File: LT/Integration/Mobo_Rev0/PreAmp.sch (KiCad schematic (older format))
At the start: 8 parts, among them Q2 5486

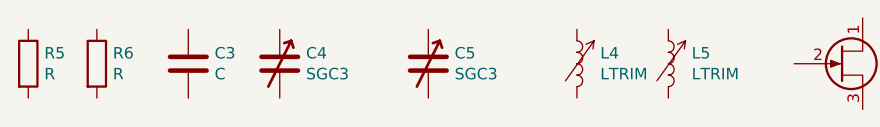
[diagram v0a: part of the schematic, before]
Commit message: I uploaded the schematics for the receiving stage into their respective hierarchial sheets and have begun the integration of the received stage
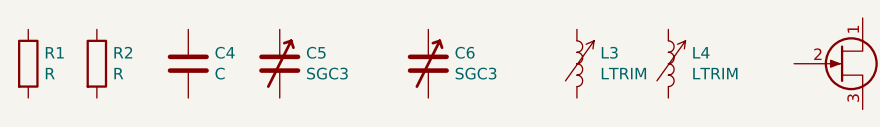
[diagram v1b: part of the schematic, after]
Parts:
- C4: renamed from C3; footprint Capacitor_SMD:C_0805_2012Metric -> (none)
- C5: renamed from C4; footprint LT:CAP_trimmer_SGC3_Download -> (none)
- C6: renamed from C5; footprint LT:CAP_trimmer_SGC3_Download -> (none)
- L3: renamed from L4; footprint LT:IND_trimmer_7M3 -> (none)
- L4: renamed from L5; footprint LT:IND_trimmer_7M3 -> (none)
- Q2: footprint Package_TO_SOT_SMD:TSOT-23 -> (none)
- renumbered R5 to R1, R6 to R2
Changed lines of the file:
@@
 $EndDescr
 $Comp
-L Device:R R5
+L Device:R R1
 U 1 1 5E4C437D
 P 2150 1950
-F 0 "R5" H 2220 1996 50  0000 L CNN
+F 0 "R1" H 2220 1996 50  0000 L CNN
 F 1 "R" H 2220 1905 50  0000 L CNN
 F 2 "Capacitor_SMD:C_0805_2012Metric" V 2080 1950 50  0001 C CNN
@@
 $EndComp
 $Comp
-L Device:R R6
+L Device:R R2
 U 1 1 5E4C43C9
 P 2450 1950
-F 0 "R6" H 2520 1996 50  0000 L CNN
+F 0 "R2" H 2520 1996 50  0000 L CNN
 F 1 "R" H 2520 1905 50  0000 L CNN
 F 2 "Capacitor_SMD:C_0805_2012Metric" V 2380 1950 50  0001 C CNN
@@
 $EndComp
 $Comp
-L Device:C C3
+L Device:C C4
 U 1 1 5E4C4423
 P 2850 1950
-F 0 "C3" H 2965 1996 50  0000 L CNN
+F 0 "C4" H 2965 1996 50  0000 L CNN
 F 1 "C" H 2965 1905 50  0000 L CNN
-F 2 "Capacitor_SMD:C_0805_2012Metric" H 2888 1800 50  0001 C CNN
+F 2 "" H 2888 1800 50  0001 C CNN
 F 3 "~" H 2850 1950 50  0001 C CNN
 	1    2850 1950
@@
 $EndComp
 $Comp
-L Device:C_Variable C4
+L Device:C_Variable C5
 U 1 1 5E4C44A9
 P 3250 1950
-F 0 "C4" H 3365 1996 50  0000 L CNN
+F 0 "C5" H 3365 1996 50  0000 L CNN
 F 1 "SGC3" H 3365 1905 50  0000 L CNN
-F 2 "LT:CAP_trimmer_SGC3_Download" H 3250 1950 50  0001 C CNN
+F 2 "" H 3250 1950 50  0001 C CNN
 F 3 "~" H 3250 1950 50  0001 C CNN
 	1    3250 1950
@@
 $EndComp
 $Comp
-L Device:C_Variable C5
+L Device:C_Variable C6
 U 1 1 5E4C44E9
 P 3900 1950
-F 0 "C5" H 4015 1996 50  0000 L CNN
+F 0 "C6" H 4015 1996 50  0000 L CNN
 F 1 "SGC3" H 4015 1905 50  0000 L CNN
-F 2 "LT:CAP_trimmer_SGC3_Download" H 3900 1950 50  0001 C CNN
+F 2 "" H 3900 1950 50  0001 C CNN
 F 3 "~" H 3900 1950 50  0001 C CNN
 	1    3900 1950
@@
 $EndComp
 $Comp
-L Device:LTRIM L4
+L Device:LTRIM L3
 U 1 1 5E4C4541
 P 4550 1950
-F 0 "L4" H 4652 1996 50  0000 L CNN
+F 0 "L3" H 4652 1996 50  0000 L CNN
 F 1 "LTRIM" H 4652 1905 50  0000 L CNN
-F 2 "LT:IND_trimmer_7M3" H 4550 1950 50  0001 C CNN
+F 2 "" H 4550 1950 50  0001 C CNN
 F 3 "~" H 4550 1950 50  0001 C CNN
 	1    4550 1950
@@
 $EndComp
 $Comp
-L Device:LTRIM L5
+L Device:LTRIM L4
 U 1 1 5E4C459D
 P 4950 1950
-F 0 "L5" H 5052 1996 50  0000 L CNN
+F 0 "L4" H 5052 1996 50  0000 L CNN
 F 1 "LTRIM" H 5052 1905 50  0000 L CNN
-F 2 "LT:IND_trimmer_7M3" H 4950 1950 50  0001 C CNN
+F 2 "" H 4950 1950 50  0001 C CNN
 F 3 "~" H 4950 1950 50  0001 C CNN
 	1    4950 1950
@@
 F 0 "Q2" H 5891 1996 50  0000 L CNN
 F 1 "5486" H 5891 1905 50  0000 L CNN
-F 2 "Package_TO_SOT_SMD:TSOT-23" H 5900 2050 50  0001 C CNN
+F 2 "" H 5900 2050 50  0001 C CNN
 F 3 "~" H 5700 1950 50  0001 C CNN
 	1    5700 1950

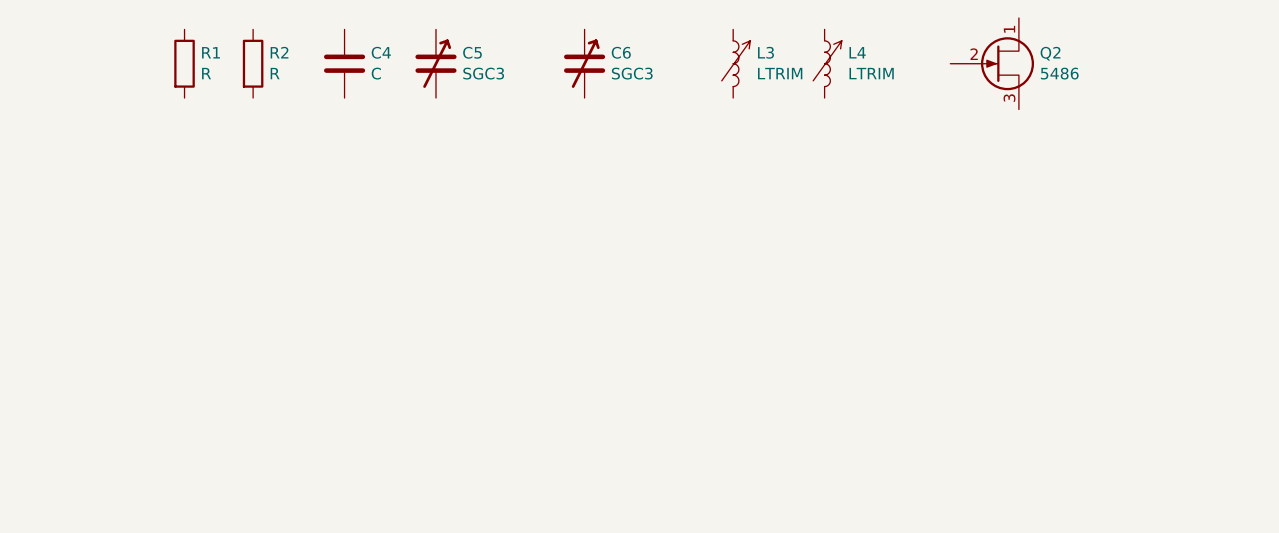
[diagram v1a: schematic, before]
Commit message: Finished a preliminary layout for the Receiving Stage, and uploaded the schematics for the Pre-Amp, 29.4 BPF, and 29.4 LPF.
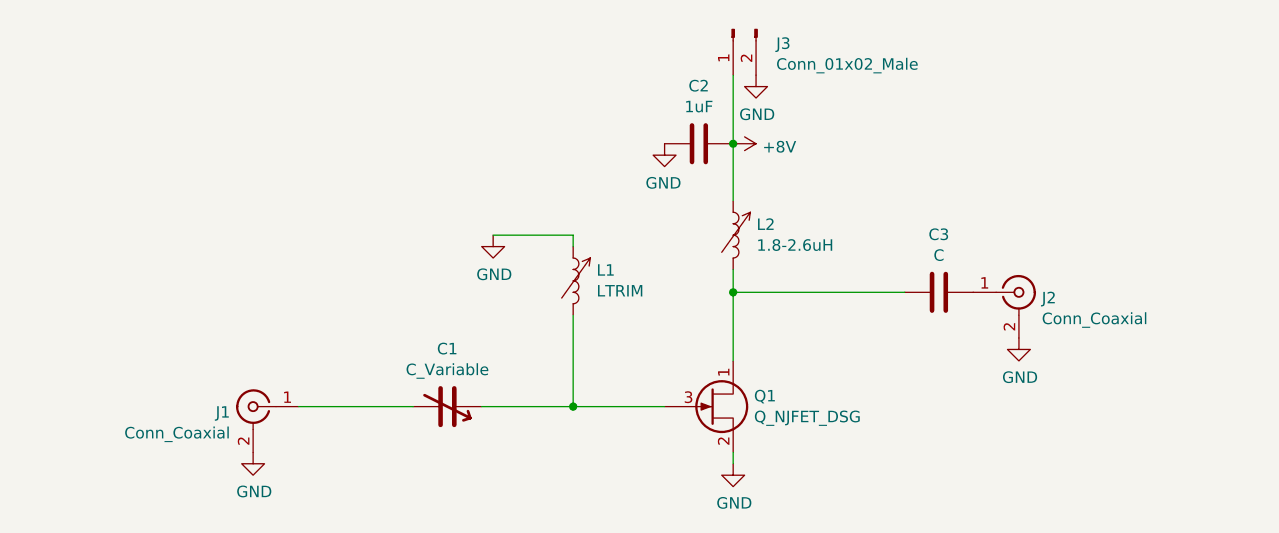
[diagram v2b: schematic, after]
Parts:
- removed C4: C, symbol Device:C
- removed C5, C6: SGC3, symbol Device:C_Variable
- removed L3, L4: LTRIM, symbol Device:LTRIM
- removed Q2: 5486, symbol Device:Q_NJFET_DGS
- removed R1, R2: R, Capacitor_SMD:C_0805_2012Metric, symbol Device:R
- added C1: C_Variable, LT:CAP_trimmer_SGC3_Download, symbol Device:C_Variable
- added C2: 1uF, Capacitor_SMD:C_0805_2012Metric_Pad1.15x1.40mm_HandSolder, symbol Device:C
- added C3: C, Capacitor_SMD:C_0805_2012Metric_Pad1.15x1.40mm_HandSolder, symbol Device:C
- added J1, J2: Conn_Coaxial, Connector_Coaxial:SMA_Amphenol_132289_EdgeMount, symbol Connector:Conn_Coaxial
- added J3: Conn_01x02_Male, Connector_PinHeader_2.54mm:PinHeader_1x02_P2.54mm_Vertical, symbol Connector:Conn_01x02_Male
- added L1: LTRIM, LT:IND_trimmer_7M3, symbol Device:LTRIM
- added L2: 1.8-2.6uH, LT:IND_trimmer_7M3, symbol Device:LTRIM
- added Q1: Q_NJFET_DSG, Package_TO_SOT_SMD:SOT-23, symbol Device:Q_NJFET_DSG
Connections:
- new net: C1.1, L1.2, Q1.3 (G)
- new net: C3.2, L2.2, Q1.1 (D)
- new net: C1.2, J1.1 (In)
- new net: C3.1, J2.1 (In)
- new net +8V: C2.1, J3.1 (Pin_1), L2.1
- new net GND: C2.2, J1.2 (Ext), J2.2 (Ext), J3.2 (Pin_2), L1.1, Q1.2 (S)

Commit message: Annotating components for Transmitting stage. In progress
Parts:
- renumbered C1 to C33, C2 to C34, C3 to C35
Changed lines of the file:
@@
 $Descr A4 11693 8268
 encoding utf-8
-Sheet 1 10
+Sheet 3 10
 Title ""
 Date ""
@@
 $EndComp
 $Comp
-L Device:C C2
+L Device:C C34
 U 1 1 5E544C2E
 P 4400 2300
-F 0 "C2" V 4652 2300 50  0000 C CNN
+F 0 "C34" V 4652 2300 50  0000 C CNN
 F 1 "1uF" V 4561 2300 50  0000 C CNN
 F 2 "Capacitor_SMD:C_0805_2012Metric_Pad1.15x1.40mm_HandSolder" H 4438 2150 50  0001 C CNN
@@
 $EndComp
 $Comp
-L Device:C_Variable C1
+L Device:C_Variable C33
 U 1 1 5E545231
 P 3300 3450
-F 0 "C1" V 3048 3450 50  0000 C CNN
+F 0 "C33" V 3048 3450 50  0000 C CNN
 F 1 "C_Variable" V 3139 3450 50  0000 C CNN
 F 2 "LT:CAP_trimmer_SGC3_Download" H 3300 3450 50  0001 C CNN
@@
 Connection ~ 3850 3450
 $Comp
-L Device:C C3
+L Device:C C35
 U 1 1 5E54F603
 P 5450 2950
-F 0 "C3" V 5198 2950 50  0000 C CNN
+F 0 "C35" V 5198 2950 50  0000 C CNN
 F 1 "C" V 5289 2950 50  0000 C CNN
 F 2 "Capacitor_SMD:C_0805_2012Metric_Pad1.15x1.40mm_HandSolder" H 5488 2800 50  0001 C CNN

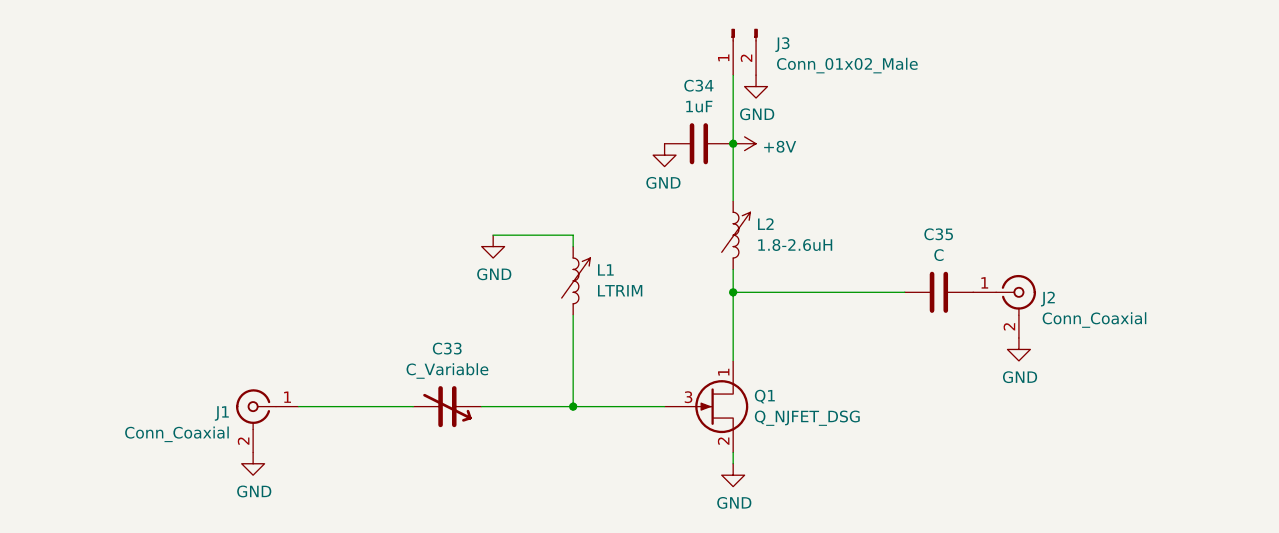
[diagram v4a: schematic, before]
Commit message: Transmitting stage annotations are done. Ready to layout PCB for rev0
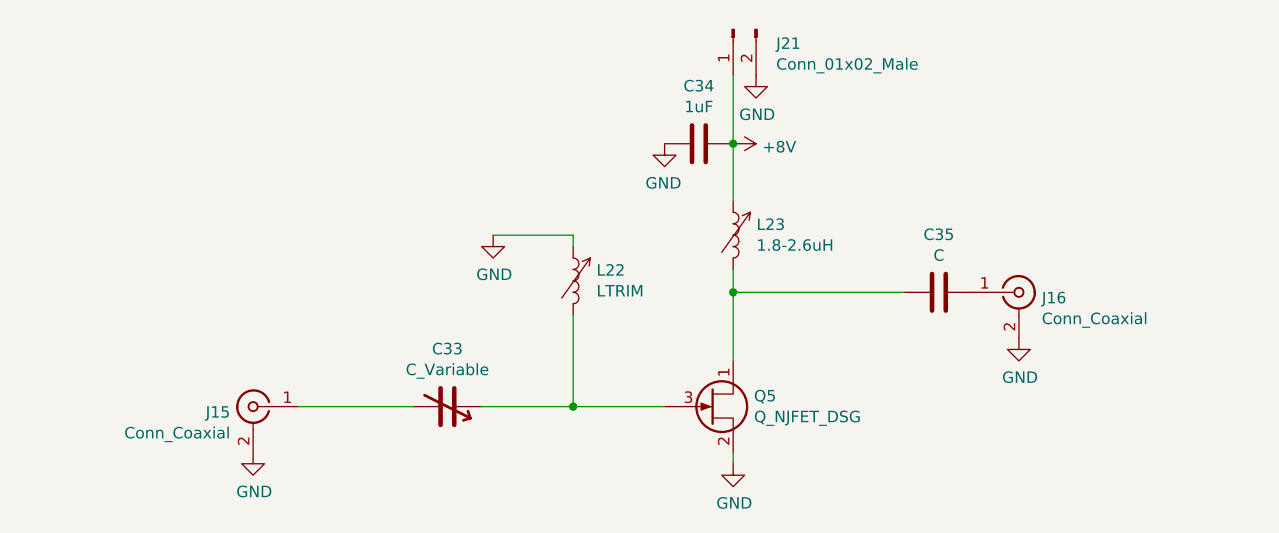
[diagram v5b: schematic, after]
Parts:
- renumbered J1 to J15, J2 to J16, J3 to J21, L1 to L22, L2 to L23, Q1 to Q5
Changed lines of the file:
@@
 $EndDescr
 $Comp
-L Device:LTRIM L1
+L Device:LTRIM L22
 U 1 1 5E543F18
 P 3850 2900
-F 0 "L1" H 3952 2946 50  0000 L CNN
+F 0 "L22" H 3952 2946 50  0000 L CNN
 F 1 "LTRIM" H 3952 2855 50  0000 L CNN
 F 2 "LT:IND_trimmer_7M3" H 3850 2900 50  0001 C CNN
@@
 $EndComp
 $Comp
-L Device:LTRIM L2
+L Device:LTRIM L23
 U 1 1 5E54443E
 P 4550 2700
-F 0 "L2" H 4652 2746 50  0000 L CNN
+F 0 "L23" H 4652 2746 50  0000 L CNN
 F 1 "1.8-2.6uH" H 4652 2655 50  0000 L CNN
 F 2 "LT:IND_trimmer_7M3" H 4550 2700 50  0001 C CNN
@@
 $EndComp
 $Comp
-L Connector:Conn_Coaxial J1
+L Connector:Conn_Coaxial J15
 U 1 1 5E546B8B
 P 2450 3450
-F 0 "J1" H 2550 3425 50  0000 L CNN
+F 0 "J15" H 2550 3425 50  0000 L CNN
 F 1 "Conn_Coaxial" H 2550 3334 50  0000 L CNN
 F 2 "Connector_Coaxial:SMA_Amphenol_132289_EdgeMount" H 2450 3450 50  0001 C CNN
@@
 $EndComp
 $Comp
-L Connector:Conn_Coaxial J2
+L Connector:Conn_Coaxial J16
 U 1 1 5E547249
 P 5800 2950
-F 0 "J2" H 5900 2925 50  0000 L CNN
+F 0 "J16" H 5900 2925 50  0000 L CNN
 F 1 "Conn_Coaxial" H 5900 2834 50  0000 L CNN
 F 2 "Connector_Coaxial:SMA_Amphenol_132289_EdgeMount" H 5800 2950 50  0001 C CNN
@@
 	4550 2950 4550 3250
 $Comp
-L Device:Q_NJFET_DSG Q1
+L Device:Q_NJFET_DSG Q5
 U 1 1 5E56089D
 P 4450 3450
-F 0 "Q1" H 4641 3496 50  0000 L CNN
+F 0 "Q5" H 4641 3496 50  0000 L CNN
 F 1 "Q_NJFET_DSG" H 4641 3405 50  0000 L CNN
 F 2 "Package_TO_SOT_SMD:SOT-23" H 4650 3550 50  0001 C CNN
@@
 	3850 3450 4250 3450
 $Comp
-L Connector:Conn_01x02_Male J3
+L Connector:Conn_01x02_Male J21
 U 1 1 5E565458
 P 4550 1800
-F 0 "J3" V 4612 1612 50  0000 R CNN
+F 0 "J21" V 4612 1612 50  0000 R CNN
 F 1 "Conn_01x02_Male" V 4703 1612 50  0000 R CNN
 F 2 "Connector_PinHeader_2.54mm:PinHeader_1x02_P2.54mm_Vertical" H 4550 1800 50  0001 C CNN

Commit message: Working on Transmitting Stage rev 0 integration board. Still in progress
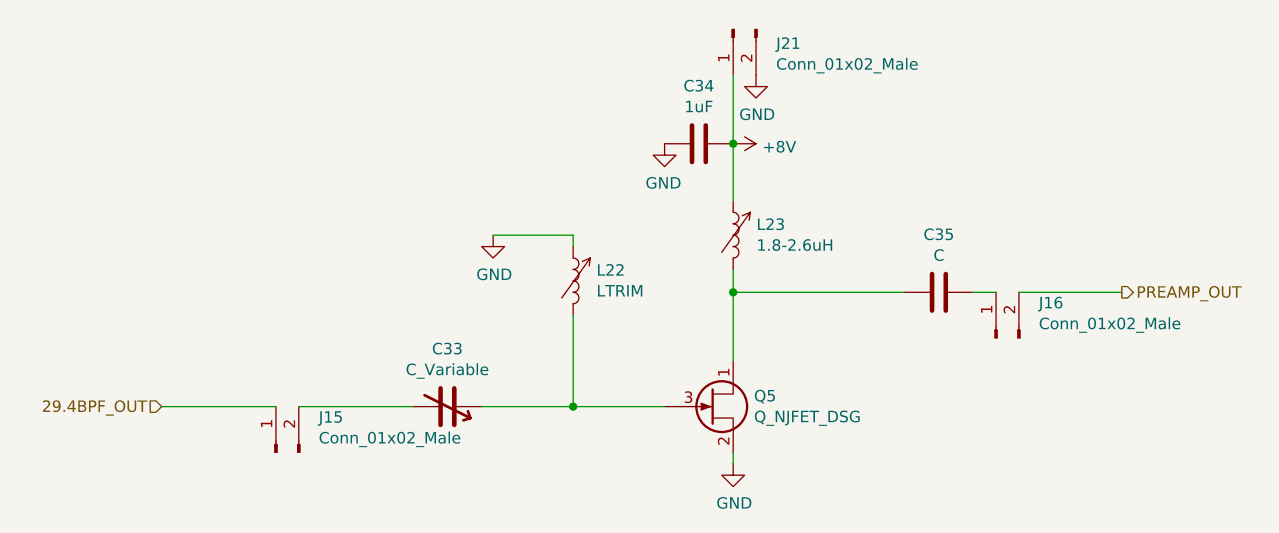
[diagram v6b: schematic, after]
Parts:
- removed J15, J16: Conn_Coaxial, Connector_Coaxial:SMA_Amphenol_132289_EdgeMount, symbol Connector:Conn_Coaxial
- added J15, J16: Conn_01x02_Male, Connector_PinHeader_2.54mm:PinHeader_1x02_P2.54mm_Vertical, symbol Connector:Conn_01x02_Male
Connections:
- net at C33.2: now also J15.2 (Pin_2)
- net at C35.1: now also J16.1 (Pin_1)
- new net 29.4BPF_OUT: J15.1 (Pin_1)
- new net PREAMP_OUT: J16.2 (Pin_2)
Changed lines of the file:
@@
 	0    1    1    0
 $EndComp
-$Comp
-L Connector:Conn_Coaxial J15
-U 1 1 5E546B8B
-P 2450 3450
-F 0 "J15" H 2550 3425 50  0000 L CNN
-F 1 "Conn_Coaxial" H 2550 3334 50  0000 L CNN
-F 2 "Connector_Coaxial:SMA_Amphenol_132289_EdgeMount" H 2450 3450 50  0001 C CNN
-F 3 " ~" H 2450 3450 50  0001 C CNN
-	1    2450 3450
-	-1   0    0    -1
-$EndComp
-$Comp
-L Connector:Conn_Coaxial J16
-U 1 1 5E547249
-P 5800 2950
-F 0 "J16" H 5900 2925 50  0000 L CNN
-F 1 "Conn_Coaxial" H 5900 2834 50  0000 L CNN
-F 2 "Connector_Coaxial:SMA_Amphenol_132289_EdgeMount" H 5800 2950 50  0001 C CNN
-F 3 " ~" H 5800 2950 50  0001 C CNN
-	1    5800 2950
-	1    0    0    -1
-$EndComp
-Wire Wire Line
-	2650 3450 3150 3450
 Wire Wire Line
 	3450 3450 3850 3450
@@
 	1    5450 2950
 	0    1    1    0
-$EndComp
-$Comp
-L power:GND #PWR0101
-U 1 1 5E552838
-P 2450 3650
-F 0 "#PWR0101" H 2450 3400 50  0001 C CNN
-F 1 "GND" H 2455 3477 50  0000 C CNN
-F 2 "" H 2450 3650 50  0001 C CNN
-F 3 "" H 2450 3650 50  0001 C CNN
-	1    2450 3650
-	1    0    0    -1
-$EndComp
-$Comp
-L power:GND #PWR0102
-U 1 1 5E552F6B
-P 5800 3150
-F 0 "#PWR0102" H 5800 2900 50  0001 C CNN
-F 1 "GND" H 5805 2977 50  0000 C CNN
-F 2 "" H 5800 3150 50  0001 C CNN
-F 3 "" H 5800 3150 50  0001 C CNN
-	1    5800 3150
-	1    0    0    -1
 $EndComp
 $Comp
@@
 Wire Wire Line
 	4550 2300 4550 2550
+Text HLabel 2050 3450 0    50   Input ~ 0
+29.4BPF_OUT
+Wire Wire Line
+	2050 3450 2550 3450
+Text HLabel 6250 2950 2    50   Output ~ 0
+PREAMP_OUT
+Wire Wire Line
+	5800 2950 6250 2950
+$Comp
+L Connector:Conn_01x02_Male J15
+U 1 1 5EA03203
+P 2550 3650
+F 0 "J15" V 2703 3463 50  0000 R CNN
+F 1 "Conn_01x02_Male" V 2612 3463 50  0000 R CNN
+F 2 "Connector_PinHeader_2.54mm:PinHeader_1x02_P2.54mm_Vertical" H 2550 3650 50  0001 C CNN
+F 3 "~" H 2550 3650 50  0001 C CNN
+	1    2550 3650
+	0    -1   -1   0
+$EndComp
+Wire Wire Line
+	2650 3450 3150 3450
+Wire Wire Line
+	5600 2950 5700 2950
+$Comp
+L Connector:Conn_01x02_Male J16
+U 1 1 5EA03C2C
+P 5700 3150
+F 0 "J16" V 5853 2963 50  0000 R CNN
+F 1 "Conn_01x02_Male" V 5762 2963 50  0000 R CNN
+F 2 "Connector_PinHeader_2.54mm:PinHeader_1x02_P2.54mm_Vertical" H 5700 3150 50  0001 C CNN
+F 3 "~" H 5700 3150 50  0001 C CNN
+	1    5700 3150
+	0    -1   -1   0
+$EndComp
 $EndSCHEMATC

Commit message: Finished 29.4 MHz BPF PCB Layout. 1/4 boards complete for transmitting stage integration
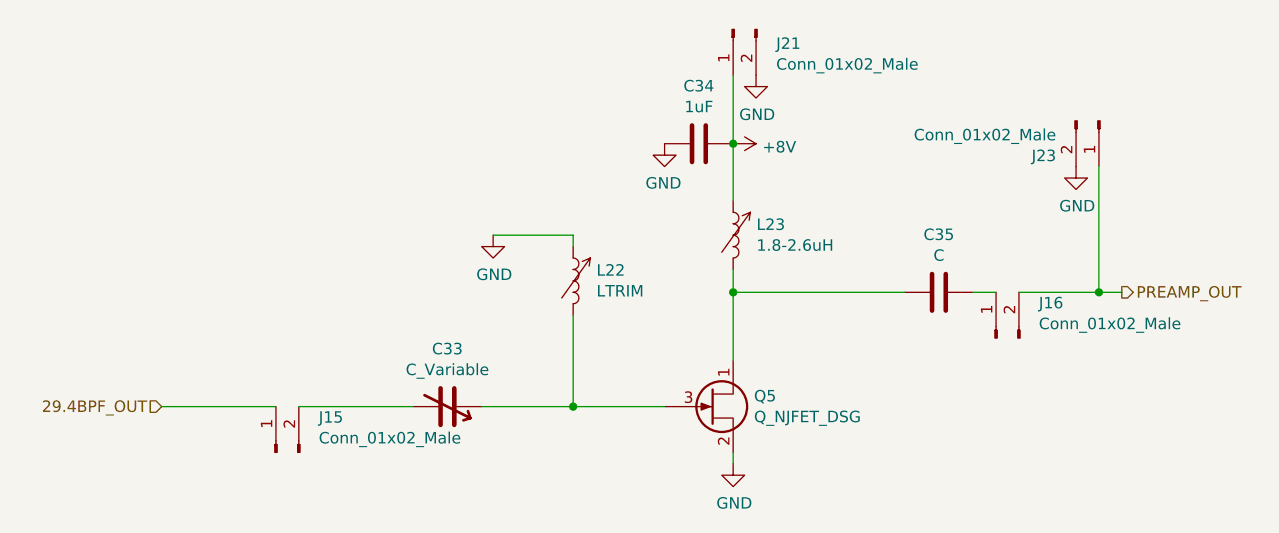
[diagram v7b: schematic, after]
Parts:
- added J23: Conn_01x02_Male, Connector_Coaxial:SMA_Amphenol_132289_EdgeMount, symbol Connector:Conn_01x02_Male
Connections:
- net GND: now also J23.2 (Pin_2)
- net PREAMP_OUT: now also J23.1 (Pin_1)
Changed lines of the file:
@@
 PREAMP_OUT
 Wire Wire Line
-	5800 2950 6250 2950
+	5800 2950 6150 2950
 $Comp
 L Connector:Conn_01x02_Male J15
@@
 	0    -1   -1   0
 $EndComp
+$Comp
+L Connector:Conn_01x02_Male J23
+U 1 1 5E9FD848
+P 6150 2200
+F 0 "J23" V 6303 2013 50  0000 R CNN
+F 1 "Conn_01x02_Male" V 6212 2013 50  0000 R CNN
+F 2 "Connector_Coaxial:SMA_Amphenol_132289_EdgeMount" H 6150 2200 50  0001 C CNN
+F 3 "~" H 6150 2200 50  0001 C CNN
+	1    6150 2200
+	0    1    1    0
+$EndComp
+Wire Wire Line
+	6150 2400 6150 2950
+Connection ~ 6150 2950
+Wire Wire Line
+	6150 2950 6250 2950
+$Comp
+L power:GND #PWR0101
+U 1 1 5E9FD99D
+P 6050 2400
+F 0 "#PWR0101" H 6050 2150 50  0001 C CNN
+F 1 "GND" H 6055 2227 50  0000 C CNN
+F 2 "" H 6050 2400 50  0001 C CNN
+F 3 "" H 6050 2400 50  0001 C CNN
+	1    6050 2400
+	1    0    0    -1
+$EndComp
 $EndSCHEMATC
